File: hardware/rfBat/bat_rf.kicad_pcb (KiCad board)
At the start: 2 copper layers, 89.8 x 41.5 mm, 86 parts, among them J1 USB_C_Receptacle_PowerOnly_6P, J2 Conn_01x04, J3 Conn_01x02_Socket, Q1 NMOS, Q2 PMOS, Q3 NMOS, SW2 RESET, SW3 SW_MEC_5E, U1 ESP8684-WROOM-01C, U2 IP2325_5M_WHJC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

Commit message: update rfBat pcb
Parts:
- added D3: LED, LED_SMD:LED_0603_1608Metric_Pad1.05x0.95mm_HandSolder, F.Cu at (67.0, 104.0)
- added D4: LED, LED_SMD:LED_0603_1608Metric_Pad1.05x0.95mm_HandSolder, F.Cu at (151.5, 104.0)
- added R15: 1k, Resistor_SMD:R_0603_1608Metric_Pad0.98x0.95mm_HandSolder, B.Cu at (144.0, 102.0)
- added R5: 1k, Resistor_SMD:R_0603_1608Metric_Pad0.98x0.95mm_HandSolder, B.Cu at (73.0, 104.5)
- moved C27 12.0 mm to (142.5, 94.5), turned to -90 degrees
- moved FB1 4.25 mm to (84.5, 83.5)
- moved C15 3.94 mm to (86.1, 86.9)
- moved C7 3.94 mm to (89.3, 84.2)
- moved C8 3.94 mm to (89.3, 91.5)
- moved C9 3.94 mm to (89.5, 89.6)
- moved U3 3.94 mm to (89.5, 87.0)
- moved J2 3.28 mm to (127.0, 79.5)
- moved C37 1.90 mm to (91.1, 105.7)
- moved R10 1.90 mm to (91.1, 104.0)
- moved R14 1.90 mm to (94.6, 105.8)
- moved R9 1.90 mm to (94.6, 104.0)
- moved SW2 1.78 mm to (137.5, 101.5)
- moved C40 1.12 mm to (131.3, 92.6)
- moved U2 1.12 mm to (137.5, 92.7)
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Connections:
- C16 pad 1: Net-(U1-EN) -> /EN
- D13 pad 1: /LED -> /BLUE
- R12 pad 1: Net-(U1-EN) -> /EN
- R13 pad 1: +3V3 -> VCC
- R4 pad 1: Net-(U1-GPIO9) -> /IO9
- U1 pad 12: unconnected-(U1-GPIO18-Pad12) -> /KEY
- U1 pad 16: unconnected-(U1-GPIO7/FSPID/MTDO/LEDPWM-Pad16) -> /ESP_TX
- U1 pad 17: unconnected-(U1-GPIO8-Pad17) -> /ESP_RX
- U1 pad 18: Net-(U1-GPIO9) -> /IO9
- U1 pad 19: /beep -> unconnected-(U1-GPIO10/FSPICS0/LEDPWM-Pad19)
- U1 pad 2: /POWER_EN -> /beep
- U1 pad 20: /BAT_FB -> /YELLOW
- U1 pad 3: Net-(U1-EN) -> /EN
- U1 pad 4: /LED -> /GREEN
- U1 pad 5: /KEY -> /BAT_FB
- U1 pad 6: /ESP_TX -> /BLUE
- U1 pad 7: /ESP_RX -> /POWER_EN
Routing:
- net +5V: track 0.00 -> 259.6 mm
- net VCC: track 0.00 -> 142.2 mm, vias 0 -> 10
- net +BATT: track 2.76 -> 107.7 mm, vias 0 -> 8
- net GNDD: track 0.00 -> 103.0 mm, vias 0 -> 20
- net /BLUE: track 0.00 -> 45.2 mm, vias 0 -> 5
- net /GREEN: track 0.00 -> 44.9 mm, vias 0 -> 1
- net /YELLOW: track 0.00 -> 36.0 mm, vias 0 -> 3
- net /IO9: track 0.00 -> 26.3 mm
- net +3V3: track 0.00 -> 25.8 mm
- net /KEY: track 0.00 -> 25.8 mm
- net Net-(LED1-DI): track 0.00 -> 22.0 mm
- net Net-(LED8-DI): track 0.00 -> 20.7 mm
- net Net-(LED4-DI): track 0.00 -> 20.7 mm
- net /BAT_FB: track 0.00 -> 20.4 mm
- net Net-(LED11-DI): track 0.00 -> 19.8 mm
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- added copper zone on B.Cu, net +BATT
- added copper zone on B.Cu, net GNDD

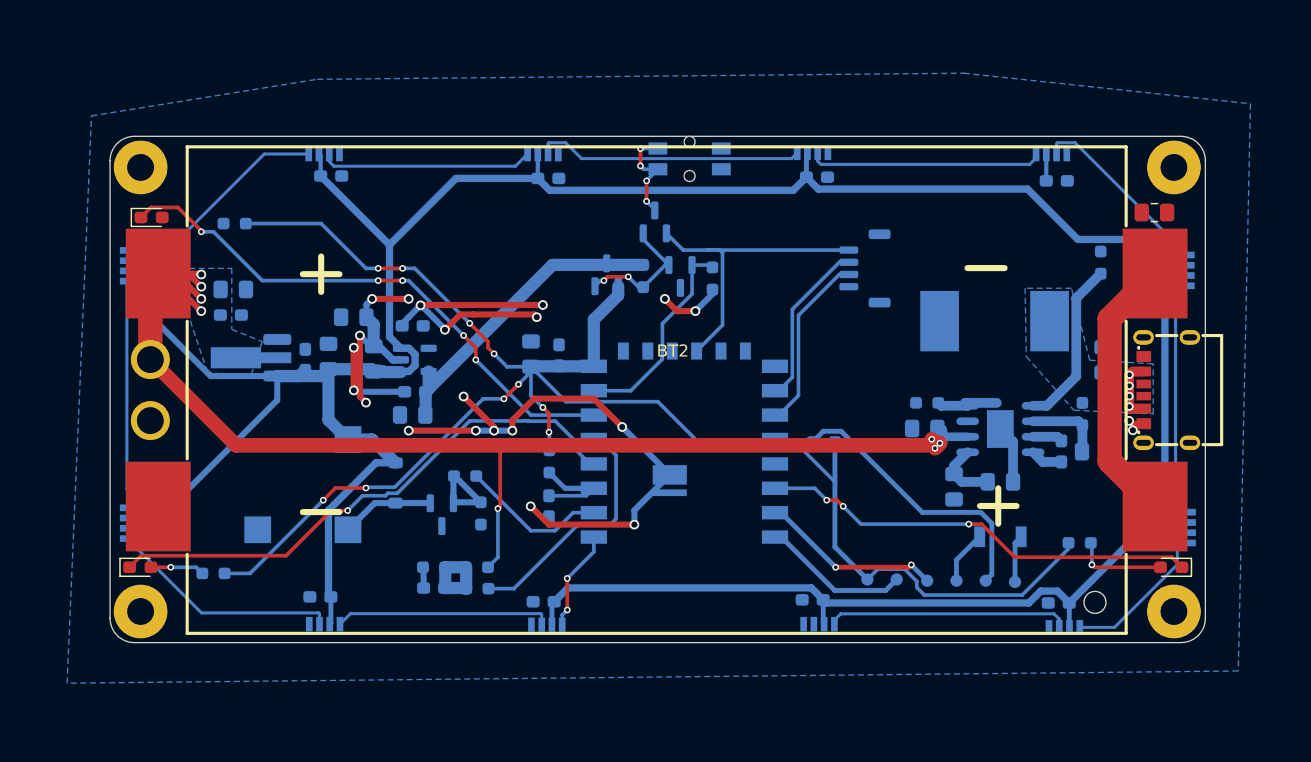
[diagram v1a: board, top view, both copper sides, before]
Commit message: rfBat ready to manufacture
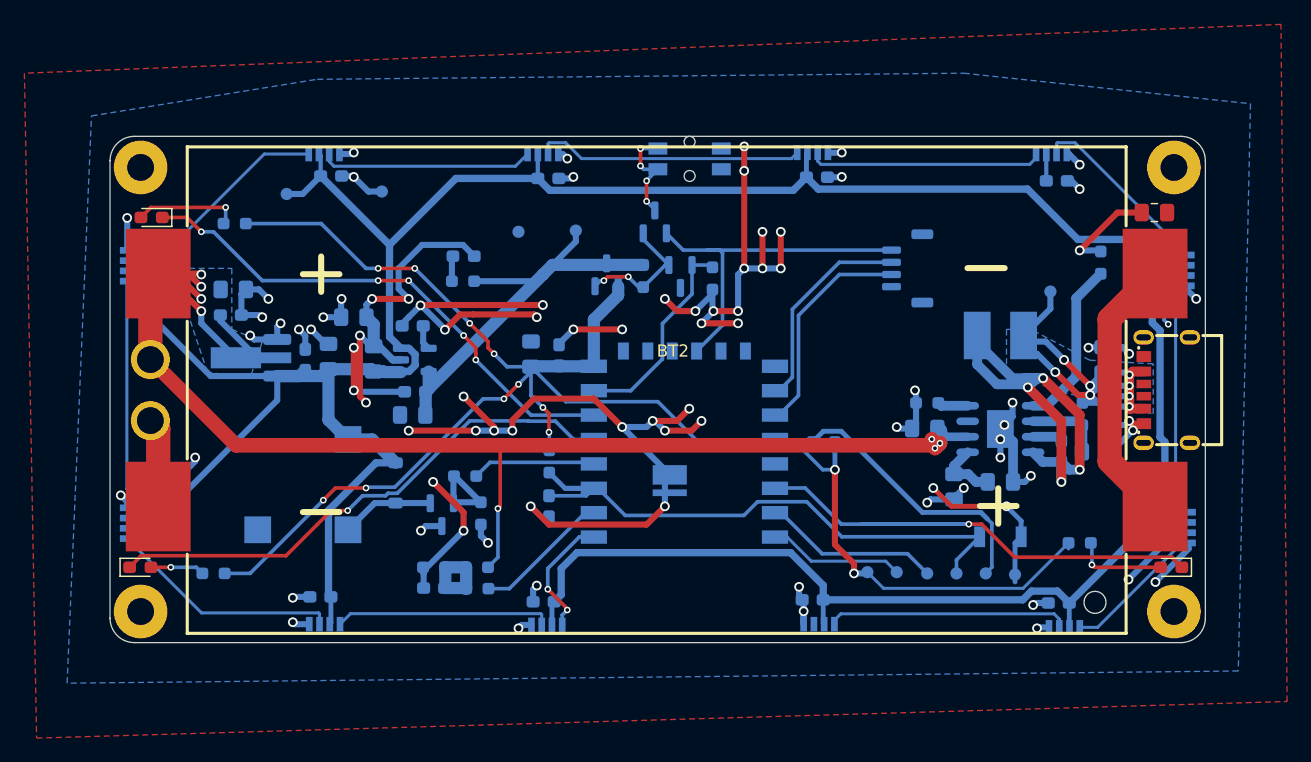
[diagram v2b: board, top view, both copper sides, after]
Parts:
- added D6: LED, LED_SMD:LED_0603_1608Metric_Pad1.05x0.95mm_HandSolder, B.Cu at (93.5, 78.5)
- added R16: 1k, Resistor_SMD:R_0603_1608Metric_Pad0.98x0.95mm_HandSolder, B.Cu at (93.5, 80.5)
- added TP10: TestPoint, TestPoint:TestPoint_Pad_D1.0mm, B.Cu at (98.0, 76.5)
- added TP12: TestPoint, TestPoint:TestPoint_Pad_D1.0mm, B.Cu at (141.6, 81.4)
- added TP7: TestPoint, TestPoint:TestPoint_Pad_D1.0mm, B.Cu at (79.0, 73.4)
- added TP8: TestPoint, TestPoint:TestPoint_Pad_D1.0mm, B.Cu at (102.7, 76.4)
- added TP9: TestPoint, TestPoint:TestPoint_Pad_D1.0mm, B.Cu at (86.8, 73.2)
- L2: footprint Inductor_SMD:L_Vishay_IHLP-4040 -> Inductor_SMD:L_Taiyo-Yuden_NR-40xx_HandSoldering
- moved J2 3.50 mm to (130.5, 79.5)
- moved L2 1.27 mm to (137.5, 85.0)
- moved TP6 0.60 mm to (138.7, 104.6)
- moved TP1 0.60 mm to (126.6, 104.4)
- moved TP2 0.60 mm to (129.0, 104.4)
- moved TP3 0.60 mm to (131.5, 104.5)
- moved TP4 0.60 mm to (133.9, 104.5)
- moved TP5 0.60 mm to (136.3, 104.5)
- turned D13 to 180 degrees
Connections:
- R6 pad 1: /beep -> /BEEP
- U1 pad 2: /beep -> /BAT_FB
- U1 pad 4: /GREEN -> /BEEP
- U1 pad 5: /BAT_FB -> /GREEN
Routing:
- net GNDPWR: track 9.90 -> 113.9 mm, vias 2 -> 46
- net GNDD: track 103.0 -> 180.8 mm, vias 20 -> 41
- net Net-(C28-Pad1): track 6.33 -> 50.1 mm, vias 4 -> 8
- net Net-(U2-LX): track 2.65 -> 40.7 mm, vias 0 -> 4
- net /EN: track 14.7 -> 48.3 mm
- net +BATT: track 107.7 -> 122.3 mm
- net /beep: track 12.1 -> 0.00 mm
- net /BEEP: track 0.00 -> 10.2 mm
- net +3V3: track 25.8 -> 35.3 mm
- net /BAT_FB: track 20.4 -> 11.2 mm
- net /YELLOW: track 36.0 -> 44.9 mm, vias 3 -> 1
- net Net-(D13-A): track 0.00 -> 8.69 mm, vias 0 -> 1
- net Net-(D2-A): track 0.00 -> 8.13 mm, vias 0 -> 1
- net +5V: track 259.6 -> 267.2 mm
- net /ESP_RX: track 14.7 -> 18.2 mm
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- added copper zone on F.Cu, net GNDPWR
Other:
- board text added: "+3V3"
- board text added: "+5V"
- board text added: "Beeper"
- board text added: "Charge"
- board text added: "ESP_RX"
- board text added: "ESP_TX"
- board text added: "GND"
- board text added: "GNDD"
- board text added: "GNDPWR"
- board text added: "KEY"
- board text added: "MCU"
- board text added: "Power"
- board text added: "USB_P"
- board text added: "V2.0"

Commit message: update rfBat
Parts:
- removed BT2: doubleBatCell, bat_rf:BAT-SMD_BH-18650-B1BA007
- removed J3: Conn_01x02_Socket, bat_rf:CONN-TH_XT30UPB-F
- added BT1: doubleBatCell, bat_rf:BAT-SMD_BH-18650-B1BA007, F.Cu at (109.7, 89.5)
- added J4: Conn_01x03, bat_rf:CONN-SMD_3P-P1.00_WAFER-SH1.0-3PWB, B.Cu at (132.5, 78.0)
- added Q4: KNY3406C, bat_rf:PDFN-8_L4.9-W5.8-P1.27-LS6.1-BL, B.Cu at (77.7, 96.4)
- added TP11: TestPoint, TestPoint:TestPoint_Pad_D1.0mm, B.Cu at (117.1, 80.3)
- J2: value Conn_01x04 -> Conn_01x02_Socket; footprint Connector_Samtec_MicroMate:Samtec_T1M-04-X-S-V_1x04-1MP_P1.0mm_Terminal_Vertical -> bat_rf:CONN-TH_XT30UPB-F; moved to F.Cu
- moved J2 63.3 mm to (68.0, 89.5)
- moved R10 42.1 mm to (123.2, 76.9), turned to -90 degrees
- moved C37 41.9 mm to (121.5, 76.9), turned to 90 degrees
- moved R9 37.1 mm to (123.2, 80.4), turned to -90 degrees
- moved R14 36.9 mm to (121.5, 80.4), turned to 90 degrees
- moved TP9 30.7 mm to (117.4, 76.2)
- moved BZ1 9.78 mm to (90.0, 95.8), turned to 90 degrees
- moved R7 9.62 mm to (87.7, 106.0), turned to 0 degrees
- moved TP7 9.04 mm to (88.0, 72.5)
- moved R6 8.64 mm to (91.8, 105.0)
- moved D5 7.22 mm to (92.7, 102.5), turned to 180 degrees
- moved Q1 5.57 mm to (87.2, 103.0), turned to 180 degrees
- moved R13 4.31 mm to (72.0, 72.5), turned to -90 degrees
- moved C1 3.64 mm to (81.5, 83.5)
- moved C15 3.64 mm to (87.1, 83.4)
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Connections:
- D13 pad 1: /BLUE -> GNDPWR
- D3 pad 1: /GREEN -> GNDPWR
- D4 pad 1: /YELLOW -> GNDPWR
- J2 pad 1: GNDD -> Net-(J2-Pin_1)
- J2 pad 2: /ESP_RX -> +BATT
- Q3 pad 3: GNDD -> GNDPWR
- R11 pad 1: GNDD -> GNDPWR
- R13 pad 1: VCC -> /BLUE
- R15 pad 1: VCC -> /YELLOW
- R5 pad 1: VCC -> /GREEN
- SW3 pad 1: GNDD -> GNDPWR
- SW3 pad 2: GNDD -> GNDPWR
- U1 pad 19: unconnected-(U1-GPIO10/FSPICS0/LEDPWM-Pad19) -> /YELLOW
- U1 pad 2: /BAT_FB -> /BEEP
- U1 pad 20: /YELLOW -> /BAT_FB
- U1 pad 4: /BEEP -> /GREEN
- U1 pad 5: /GREEN -> /BAT_EN
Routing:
- net VCC: track 141.0 -> 62.3 mm, vias 12 -> 4
- net +BATT: track 122.3 -> 150.3 mm, vias 8 -> 11
- net /BAT_EN: track 0.00 -> 27.2 mm
- net Net-(BT2-+-Pad3): track 22.2 -> 0.00 mm
- net Net-(BT1-+-Pad3): track 0.00 -> 22.2 mm
- net GNDD: track 180.8 -> 200.6 mm, vias 41 -> 20
- net /YELLOW: track 44.9 -> 26.8 mm, vias 1 -> 2
- net /KEY: track 29.3 -> 14.2 mm
- net GNDPWR: track 113.9 -> 127.8 mm, vias 46 -> 53
- net Net-(J2-Pin_1): track 0.00 -> 11.7 mm
- net /BAT_FB: track 11.2 -> 20.1 mm, vias 0 -> 4
- net /GREEN: track 44.2 -> 36.3 mm, vias 1 -> 0
- net Net-(D13-A): track 8.69 -> 3.33 mm
- net /BEEP: track 10.2 -> 14.4 mm
- net +5V: track 267.2 -> 263.0 mm, vias 0 -> 8
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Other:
- board text added: "3V3"
- board text added: "BAT"
- board text added: "GNDP"
- board text removed: "+3V3"
- board text removed: "GNDPWR"
- board text removed: "KEY"

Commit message: update pcbs
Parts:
- removed TP10: TestPoint, TestPoint:TestPoint_Pad_D1.0mm
- D13, D3, D4, D6: footprint LED_SMD:LED_0603_1608Metric_Pad1.05x0.95mm_HandSolder -> LED_SMD:LED_0402_1005Metric_Pad0.77x0.64mm_HandSolder
- D2: footprint Capacitor_SMD:C_0805_2012Metric_Pad1.18x1.45mm_HandSolder -> LED_SMD:LED_0402_1005Metric_Pad0.77x0.64mm_HandSolder
- SW2: footprint Button_Switch_SMD:SW_SPST_B3U-1000P -> Button_Switch_SMD:SW_Push_1P1T_NO_CK_KMR2
- U1: value ESP8684-WROOM-01C -> ESP32-C3-WROOM-02-N4; footprint bat_rf:WIRELM-SMD_ESP8684-WROOM0-1C -> bat_rf:BULETM-SMD_18P-L20.0-W18.0-P1.50_ESP32-C3-WROOM
- moved TP5 37.3 mm to (101.0, 92.3), turned to 0 degrees
- moved TP4 33.2 mm to (107.2, 84.7), turned to 0 degrees
- moved SW2 33.0 mm to (112.1, 80.5)
- moved TP1 30.9 mm to (96.5, 97.4), turned to 0 degrees
- moved TP6 30.6 mm to (115.4, 84.8), turned to 0 degrees
- moved R4 23.1 mm to (100.0, 91.5), turned to 90 degrees
- moved R11 18.3 mm to (95.8, 83.0), turned to -90 degrees
- moved Q3 17.9 mm to (94.7, 87.0)
- moved R8 17.7 mm to (91.9, 87.0)
- moved D1 17.5 mm to (93.1, 82.6)
- moved Q2 17.5 mm to (89.2, 86.9)
- moved TP3 17.1 mm to (122.4, 90.0), turned to 0 degrees
- moved TP8 17.0 mm to (88.7, 82.8)
- moved C13 15.4 mm to (100.0, 102.0)
- moved C12 15.4 mm to (98.2, 101.9)
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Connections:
- C14 pad 2: Net-(LED10-VDD) -> +5V
- LED10 pad 3: Net-(LED10-VDD) -> +5V
- U1 pad 1: /RGB -> VCC
- U1 pad 10: unconnected-(U1-NC-Pad10) -> /ESP_RX
- U1 pad 11: unconnected-(U1-NC-Pad11) -> /RXD
- U1 pad 12: /KEY -> /TXD
- U1 pad 13: unconnected-(U1-NC-Pad13) -> /ESP_TX
- U1 pad 15: GNDD -> /BAT_FB
- U1 pad 16: /ESP_TX -> /YELLOW
- U1 pad 17: /ESP_RX -> /BEEP
- U1 pad 18: /IO9 -> /RGB
- U1 pad 19: /YELLOW -> GNDD
- U1 pad 2: /BEEP -> /EN
- U1 pad 3: /EN -> /GREEN
- U1 pad 4: /GREEN -> /BAT_EN
- U1 pad 5: /BAT_EN -> /POWER_EN
- U1 pad 6: /BLUE -> /KEY
- U1 pad 7: /POWER_EN -> /BLUE
- U1 pad 8: VCC -> /IO9
- U1 pad 9: unconnected-(U1-NC-Pad9) -> GNDD
- U4 pad 2: +BATT -> +5V
- U4 pad 3: +5V -> +BATT
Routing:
- net GNDD: track 200.6 -> 43.3 mm, vias 20 -> 12
- net +3V3: track 36.3 -> 0.00 mm
- net VCC: track 62.3 -> 34.7 mm, vias 4 -> 0
- net +BATT: track 150.3 -> 124.1 mm, vias 11 -> 9
- net +5V: track 263.0 -> 239.2 mm, vias 8 -> 3
- net /IO9: track 25.7 -> 2.98 mm
- net Net-(SW3-A): track 8.43 -> 26.6 mm
- net /BEEP: track 14.4 -> 31.6 mm, vias 0 -> 2
- net /EN: track 48.3 -> 33.9 mm
- net /RGB: track 10.5 -> 24.0 mm
- net /BAT_FB: track 20.1 -> 9.11 mm, vias 4 -> 0
- net GNDPWR: track 127.8 -> 116.9 mm
- net /RXD: track 14.5 -> 4.29 mm
- net /TXD: track 11.7 -> 4.76 mm
- net /GREEN: track 36.3 -> 31.3 mm, vias 0 -> 2
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- added copper zone on B.Cu, net +3V3
- added copper zone on B.Cu, net +5V
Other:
- board text added: "BOOT"
- board text added: "EN"
- board text added: "RESET"
- board text added: "RXD"
- board text added: "TXD"
- board text added: "V2.1"
- board text added: "VCC"
- board text removed: "V2.0"

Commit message: f
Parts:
- removed SW2: RESET, Button_Switch_SMD:SW_Push_1P1T_NO_CK_KMR2
- added SW1: 3*4*2.5MM_贴片4脚, bat_rf:SW-SMD_4P-L4.2-W3.3-P2.15-LS5.1, B.Cu at (112.5, 77.8)
- moved TP1 21.3 mm to (113.8, 85.0)
- moved TP2 14.9 mm to (109.3, 84.9)
- moved TP6 12.4 mm to (103.0, 85.0)
- moved TP3 11.9 mm to (111.6, 85.0)
- moved TP5 8.37 mm to (105.1, 85.0)
- moved R4 1.33 mm to (100.3, 92.8)
- moved TP4 0.30 mm to (107.2, 85.0)
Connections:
- R4 pad 1: /IO9 -> Net-(U1-IO8)
- U1 pad 10: /ESP_RX -> /BLUE
- U1 pad 13: /ESP_TX -> /ESP_RX
- U1 pad 14: unconnected-(U1-IO19-Pad14) -> /ESP_TX
- U1 pad 7: /BLUE -> Net-(U1-IO8)
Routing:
- net GNDD: track 43.3 -> 67.4 mm, vias 12 -> 18
- net /BLUE: track 41.3 -> 65.0 mm
- net VCC: track 34.7 -> 57.5 mm, vias 0 -> 2
- net /TXD: track 4.76 -> 16.1 mm
- net /RXD: track 4.29 -> 13.4 mm
- net /IO9: track 2.98 -> 10.2 mm, vias 0 -> 2
- net /ESP_RX: track 14.2 -> 19.1 mm
- net Net-(U1-IO8): track 0.00 -> 2.35 mm
- net /EN: track 33.9 -> 32.3 mm
- net /ESP_TX: track 22.1 -> 23.4 mm
- net /BAT_FB: track 9.11 -> 9.76 mm
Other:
- board text added: "V2.2"
- board text removed: "V2.1"
